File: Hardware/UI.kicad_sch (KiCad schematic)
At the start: 53 parts, among them J101 USB_C_Receptacle_USB2.0_16P, J102 ST7789 LCD, J103 TC2030, J104 Expansion, Q101 AO3400A, SW101 SIQ-02FVS3, SW102 SW_Back, SW103 Reset, SW104 Boot, U101 CH32X035G8U6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

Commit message: final tweaks before routing traces
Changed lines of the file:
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@@
 	)
 	(junction
-		(at 199.39 157.48)
-		(diameter 0)
-		(color 0 0 0 0)
-	)
-	(junction
 		(at 219.71 97.79)
 		(diameter 0)
@@
 	(wire
 		(pts
-			(xy 199.39 157.48) (xy 212.09 157.48)
+			(xy 109.22 128.27) (xy 109.22 127)
 		)
 		(stroke
@@
 	(wire
 		(pts
-			(xy 109.22 128.27) (xy 109.22 127)
+			(xy 271.78 153.67) (xy 271.78 158.75)
 		)
 		(stroke
@@
 	(wire
 		(pts
-			(xy 271.78 153.67) (xy 271.78 158.75)
+			(xy 256.54 106.68) (xy 265.43 106.68)
 		)
 		(stroke
@@
 	(wire
 		(pts
-			(xy 256.54 106.68) (xy 265.43 106.68)
+			(xy 187.96 160.02) (xy 187.96 157.48)
 		)
 		(stroke
@@
 	(wire
 		(pts
+			(xy 187.96 157.48) (xy 199.39 157.48)
+		)
+		(stroke
+			(width 0)
+			(type default)
+		)
+	)
+	(wire
+		(pts
 			(xy 16.51 115.57) (xy 20.32 115.57)
 		)
@@
 	(wire
 		(pts
+			(xy 220.98 160.02) (xy 220.98 157.48)
+		)
+		(stroke
+			(width 0)
+			(type default)
+		)
+	)
+	(wire
+		(pts
 			(xy 116.84 180.34) (xy 119.38 180.34)
 		)
@@
 	(wire
 		(pts
+			(xy 212.09 157.48) (xy 220.98 157.48)
+		)
+		(stroke
+			(width 0)
+			(type default)
+		)
+	)
+	(wire
+		(pts
 			(xy 256.54 73.66) (xy 256.54 74.93)
 		)
@@
 	(wire
 		(pts
+			(xy 212.09 165.1) (xy 212.09 160.02)
+		)
+		(stroke
+			(width 0)
+			(type default)
+		)
+	)
+	(wire
+		(pts
 			(xy 247.65 26.67) (xy 256.54 26.67)
 		)
@@
 	(wire
 		(pts
-			(xy 212.09 160.02) (xy 226.06 160.02)
+			(xy 212.09 165.1) (xy 215.9 165.1)
 		)
 		(stroke
@@
 	(wire
 		(pts
-			(xy 187.96 157.48) (xy 199.39 157.48)
-		)
-		(stroke
-			(width 0)
-			(type default)
-		)
-	)
-	(wire
-		(pts
 			(xy 234.95 72.39) (xy 234.95 81.28)
 		)
@@
 	(label "UI_D-"
 		(at 66.04 41.91 0)
-		(fields_autoplaced yes)
 		(effects
 			(font
@@
 	(label "UI_VIN"
 		(at 29.21 124.46 0)
-		(fields_autoplaced yes)
 		(effects
 			(font
@@
 	(label "UI_D+"
 		(at 66.04 44.45 0)
-		(fields_autoplaced yes)
 		(effects
 			(font
@@
 		(shape input)
 		(at 151.13 67.31 0)
-		(fields_autoplaced yes)
 		(effects
 			(font
@@
 		(shape input)
 		(at 151.13 69.85 0)
-		(fields_autoplaced yes)
 		(effects
 			(font
@@
 	(symbol
 		(lib_id "power:+3V3")
-		(at 226.06 160.02 0)
+		(at 215.9 165.1 0)
 		(unit 1)
 		(exclude_from_sim no)
@@
 		(fields_autoplaced yes)
 		(property "Reference" "#PWR0135"
-			(at 226.06 163.83 0)
+			(at 215.9 168.91 0)
 			(effects
 				(font
@@
 		)
 		(property "Value" "+3V3"
-			(at 226.06 154.94 0)
+			(at 215.9 160.02 0)
 			(effects
 				(font
@@
 		)
 		(property "Footprint" ""
-			(at 226.06 160.02 0)
+			(at 215.9 165.1 0)
 			(effects
 				(font
@@
 		)
 		(property "Datasheet" ""
-			(at 226.06 160.02 0)
+			(at 215.9 165.1 0)
 			(effects
 				(font
@@
 		)
 		(property "Description" "Power symbol creates a global label with name \"+3V3\""
-			(at 226.06 160.02 0)
+			(at 215.9 165.1 0)
 			(effects
 				(font
@@
 	(symbol
 		(lib_id "power:GND")
-		(at 187.96 157.48 0)
+		(at 187.96 160.02 0)
 		(unit 1)
 		(exclude_from_sim no)
@@
 		(fields_autoplaced yes)
 		(property "Reference" "#PWR0136"
-			(at 187.96 163.83 0)
+			(at 187.96 166.37 0)
 			(effects
 				(font
@@
 		)
 		(property "Value" "GND"
-			(at 187.96 162.56 0)
+			(at 187.96 165.1 0)
 			(effects
 				(font
@@
 		)
 		(property "Footprint" ""
-			(at 187.96 157.48 0)
+			(at 187.96 160.02 0)
 			(effects
 				(font
@@
 		)
 		(property "Datasheet" ""
-			(at 187.96 157.48 0)
+			(at 187.96 160.02 0)
 			(effects
 				(font
@@
 		)
 		(property "Description" "Power symbol creates a global label with name \"GND\" , ground"
-			(at 187.96 157.48 0)
+			(at 187.96 160.02 0)
 			(effects
 				(font
@@
 					(unit 1)
 				)
+			)
+		)
+	)
+	(symbol
+		(lib_id "power:GND")
+		(at 220.98 160.02 0)
+		(unit 1)
+		(exclude_from_sim no)
+		(in_bom yes)
+		(on_board yes)
+		(dnp no)
+		(fields_autoplaced yes)
+		(property "Reference" "#PWR0149"
+			(at 220.98 166.37 0)
+			(effects
+				(font
+					(size 1.27 1.27)
+				)
+				(hide yes)
+			)
+		)
+		(property "Value" "GND"
+			(at 220.98 165.1 0)
+			(effects
+				(font
+					(size 1.27 1.27)
+				)
+			)
+		)
+		(property "Footprint" ""
+			(at 220.98 160.02 0)
+			(effects
+				(font
+					(size 1.27 1.27)
+				)
+				(hide yes)
+			)
+		)
+		(property "Datasheet" ""
+			(at 220.98 160.02 0)
+			(effects
+				(font
+					(size 1.27 1.27)
+				)
+				(hide yes)
+			)
+		)
+		(property "Description" "Power symbol creates a global label with name \"GND\" , ground"
+			(at 220.98 160.02 0)
+			(effects
+				(font
+					(size 1.27 1.27)
+				)
+				(hide yes)
+			)
+		)
+		(pin "1"
+		)
+		(instances
+			(project "USB-C PSU"
+				(path "/2795a064-4b14-4857-8c9a-fd2d32a5a222/83a45ffb-89fc-4bf0-b371-2eda7791aa05"
+					(reference "#PWR0149")
+					(unit 1)
+				)

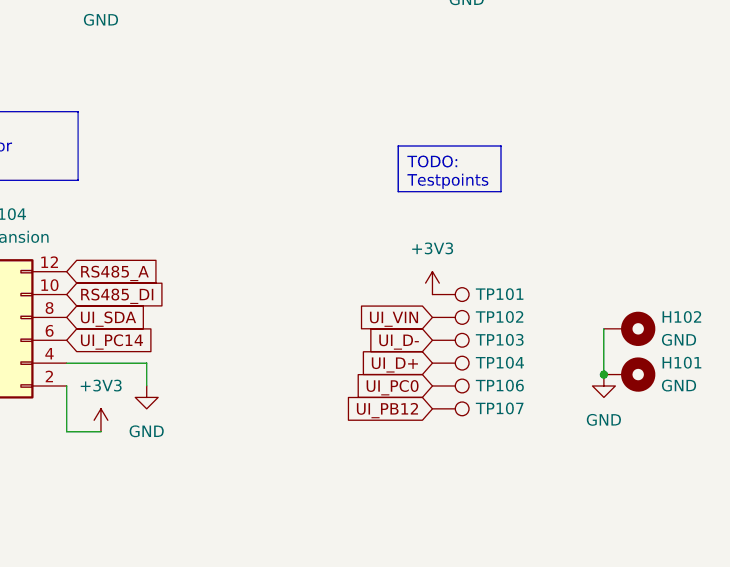
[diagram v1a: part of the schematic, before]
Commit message: UI layout done
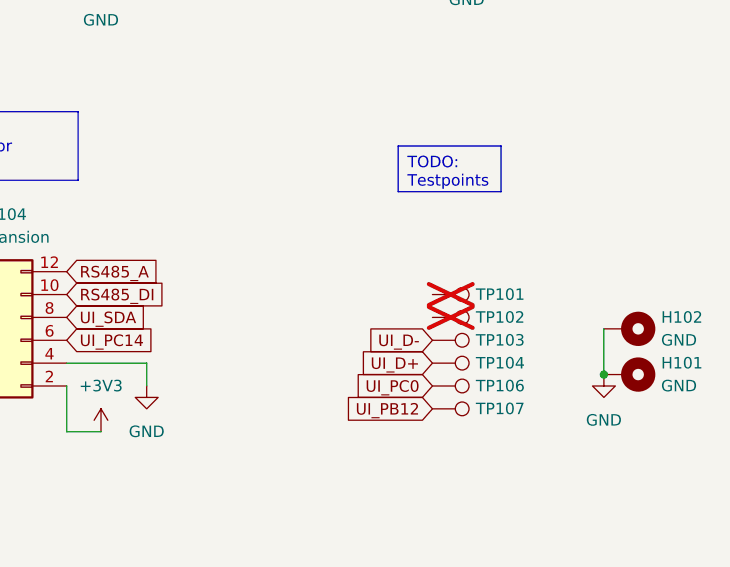
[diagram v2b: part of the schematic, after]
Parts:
- TP101, TP102: now not fitted
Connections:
- net +3V3: no longer TP101.1
- net UI_VIN: no longer TP102.1
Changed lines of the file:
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@@
 		)
 	)
-	(global_label "UI_VIN"
-		(shape input)
-		(at 252.73 152.4 180)
-		(fields_autoplaced yes)
-		(effects
-			(font
-				(size 1.27 1.27)
-			)
-			(justify right)
-		)
-		(property "Intersheetrefs" "${INTERSHEET_REFS}"
-			(at 243.818 152.4 0)
-			(effects
-				(font
-					(size 1.27 1.27)
-				)
-				(justify right)
-				(hide yes)
-			)
-		)
-	)
 	(global_label "BUZZER"
 		(shape input)
@@
 	)
 	(symbol
-		(lib_id "power:+3V3")
-		(at 252.73 149.86 0)
-		(unit 1)
-		(exclude_from_sim no)
-		(in_bom yes)
-		(on_board yes)
-		(dnp no)
-		(fields_autoplaced yes)
-		(property "Reference" "#PWR0118"
-			(at 252.73 153.67 0)
-			(effects
-				(font
-					(size 1.27 1.27)
-				)
-				(hide yes)
-			)
-		)
-		(property "Value" "+3V3"
-			(at 252.73 144.78 0)
-			(effects
-				(font
-					(size 1.27 1.27)
-				)
-			)
-		)
-		(property "Footprint" ""
-			(at 252.73 149.86 0)
-			(effects
-				(font
-					(size 1.27 1.27)
-				)
-				(hide yes)
-			)
-		)
-		(property "Datasheet" ""
-			(at 252.73 149.86 0)
-			(effects
-				(font
-					(size 1.27 1.27)
-				)
-				(hide yes)
-			)
-		)
-		(property "Description" "Power symbol creates a global label with name \"+3V3\""
-			(at 252.73 149.86 0)
-			(effects
-				(font
-					(size 1.27 1.27)
-				)
-				(hide yes)
-			)
-		)
-		(pin "1"
-		)
-		(instances
-			(project "USB-C PSU"
-				(path "/2795a064-4b14-4857-8c9a-fd2d32a5a222/83a45ffb-89fc-4bf0-b371-2eda7791aa05"
-					(reference "#PWR0118")
-					(unit 1)
-				)
-			)
-		)
-	)
-	(symbol
 		(lib_id "power:GND")
 		(at 237.49 29.21 0)
@@
 		(exclude_from_sim no)
 		(in_bom no)
-		(on_board yes)
-		(dnp no)
+		(on_board no)
+		(dnp yes)
 		(property "Reference" "TP101"
 			(at 257.556 149.86 90)
@@
 		(exclude_from_sim no)
 		(in_bom no)
-		(on_board yes)
-		(dnp no)
+		(on_board no)
+		(dnp yes)
 		(property "Reference" "TP102"
 			(at 257.556 152.4 90)

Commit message: final tweaks for v1.0
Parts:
- C101, C102: LCSC Part (none) -> C52923
- H101, H102: now not fitted
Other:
- note added: "For more cost savings, this can be replaced with discrete diodes"
- note added: "Interface for Phylion BMS will be done externally"
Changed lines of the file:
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@@
 		)
 	)
-	(text_box "TODO:\nGPIOs for Phylion"
+	(text "Interface for Phylion BMS\nwill be done externally"
 		(exclude_from_sim no)
-		(at 196.85 129.54 0)
-		(size 16.51 7.62)
-		(stroke
-			(width 0)
-			(type default)
-			(color 255 0 255 1)
-		)
-		(fill
-			(type none)
-		)
+		(at 187.452 136.398 0)
 		(effects
 			(font
-				(size 1.27 1.27)
-				(color 255 0 255 1)
+				(size 1.016 1.016)
 			)
-			(justify left top)
+			(justify left)
 		)
 	)
@@
 		)
 	)
+	(text "For more cost savings,\nthis can be replaced\nwith discrete diodes"
+		(exclude_from_sim no)
+		(at 16.256 101.092 0)
+		(effects
+			(font
+				(size 1.016 1.016)
+			)
+			(justify left)
+		)
+	)
 	(label "UI_D-"
 		(at 66.04 41.91 0)
@@
 			)
 		)
+		(property "LCSC Part" ""
+			(at 21.59 154.94 0)
+			(effects
+				(font
+					(size 1.27 1.27)
+				)
+				(hide yes)
+			)
+		)
 		(pin "1"
 		)
@@
 		(in_bom no)
 		(on_board yes)
-		(dnp no)
+		(dnp yes)
 		(fields_autoplaced yes)
 		(property "Reference" "H101"
@@
 			)
 		)
+		(property "LCSC Part" "C52923"
+			(at 58.42 129.54 0)
+			(effects
+				(font
+					(size 1.27 1.27)
+				)
+				(hide yes)
+			)
+		)
 		(pin "1"
 		)
@@
 			)
 		)
+		(property "LCSC Part" ""
+			(at 148.59 161.29 0)
+			(effects
+				(font
+					(size 1.27 1.27)
+				)
+				(hide yes)
+			)
+		)
 		(pin "1"
 		)
@@
 		(in_bom no)
 		(on_board yes)
-		(dnp no)
+		(dnp yes)
 		(fields_autoplaced yes)
 		(property "Reference" "H102"
@@
 			)
 		)
+		(property "LCSC Part" ""
+			(at 143.51 24.13 0)
+			(effects
+				(font
+					(size 1.27 1.27)
+				)
+				(hide yes)
+			)
+		)
 		(pin "1"
 		)
@@
 			(at 35.56 129.54 0)
 			(effects
+				(font
+					(size 1.27 1.27)
+				)
+				(hide yes)
+			)
+		)
+		(property "LCSC Part" "C52923"
+			(at 35.56 129.54 0)
+			(effects
